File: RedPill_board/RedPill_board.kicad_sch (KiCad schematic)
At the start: 52 parts, among them J1 USB_C_Receptacle_USB2.0, J2 PROG, Q1 S9013, SW1 RESET, U1 FCM32F103CBT6, U2 STM32F401RCT6, U4 ME6211C33M5G-N, Y1 8MHz, Y2 8MHz

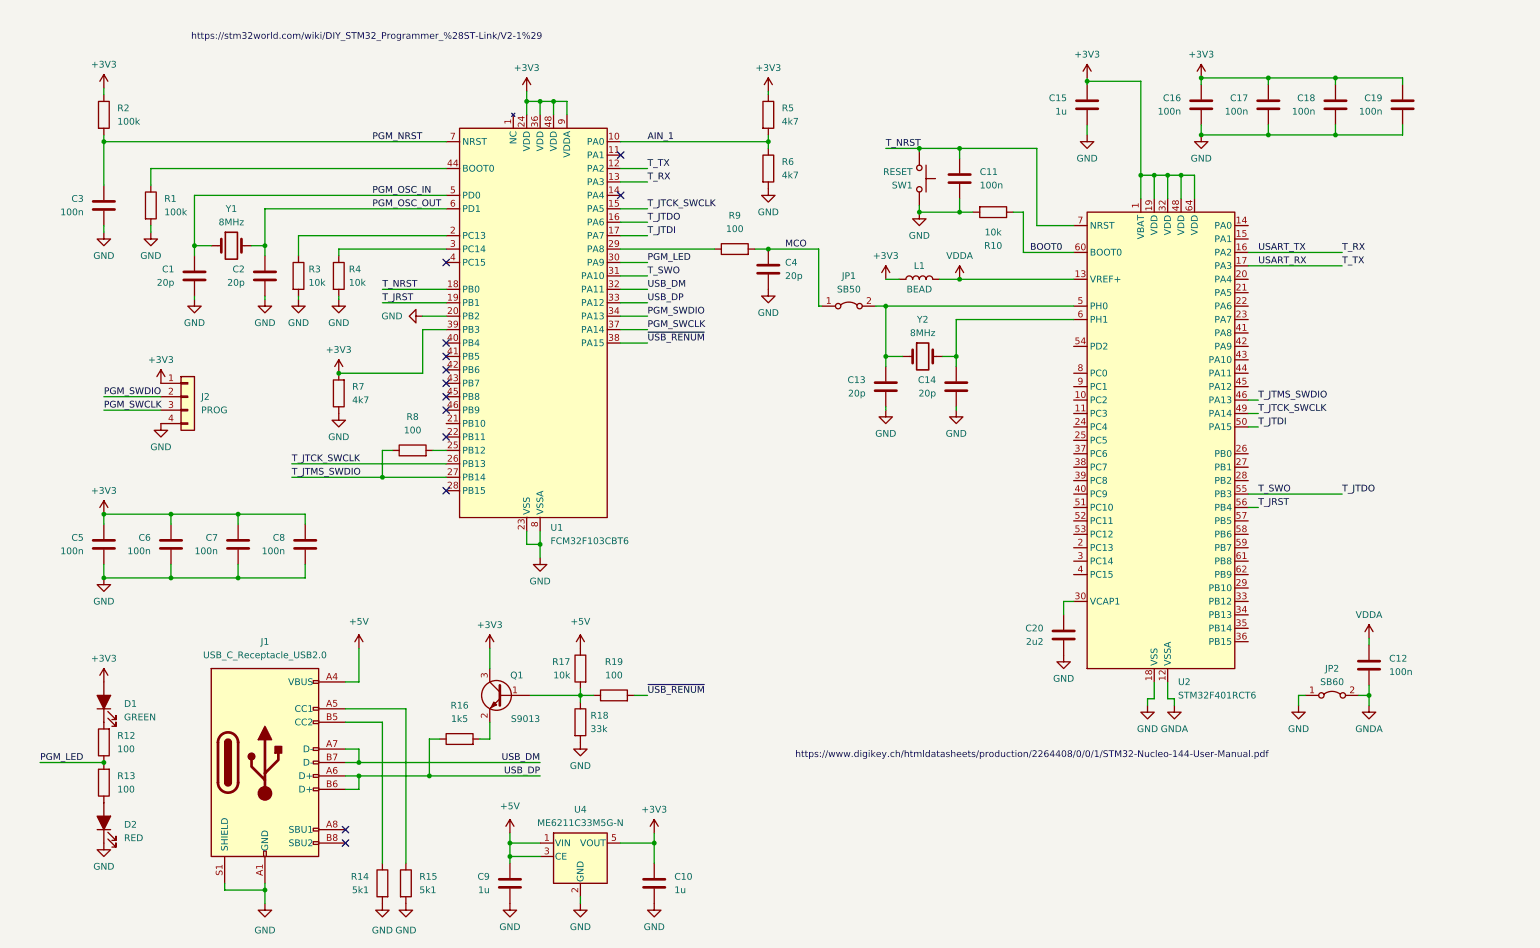
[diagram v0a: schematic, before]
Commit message: Cleanup programming nets and components, add blank connectors and initial pcb design
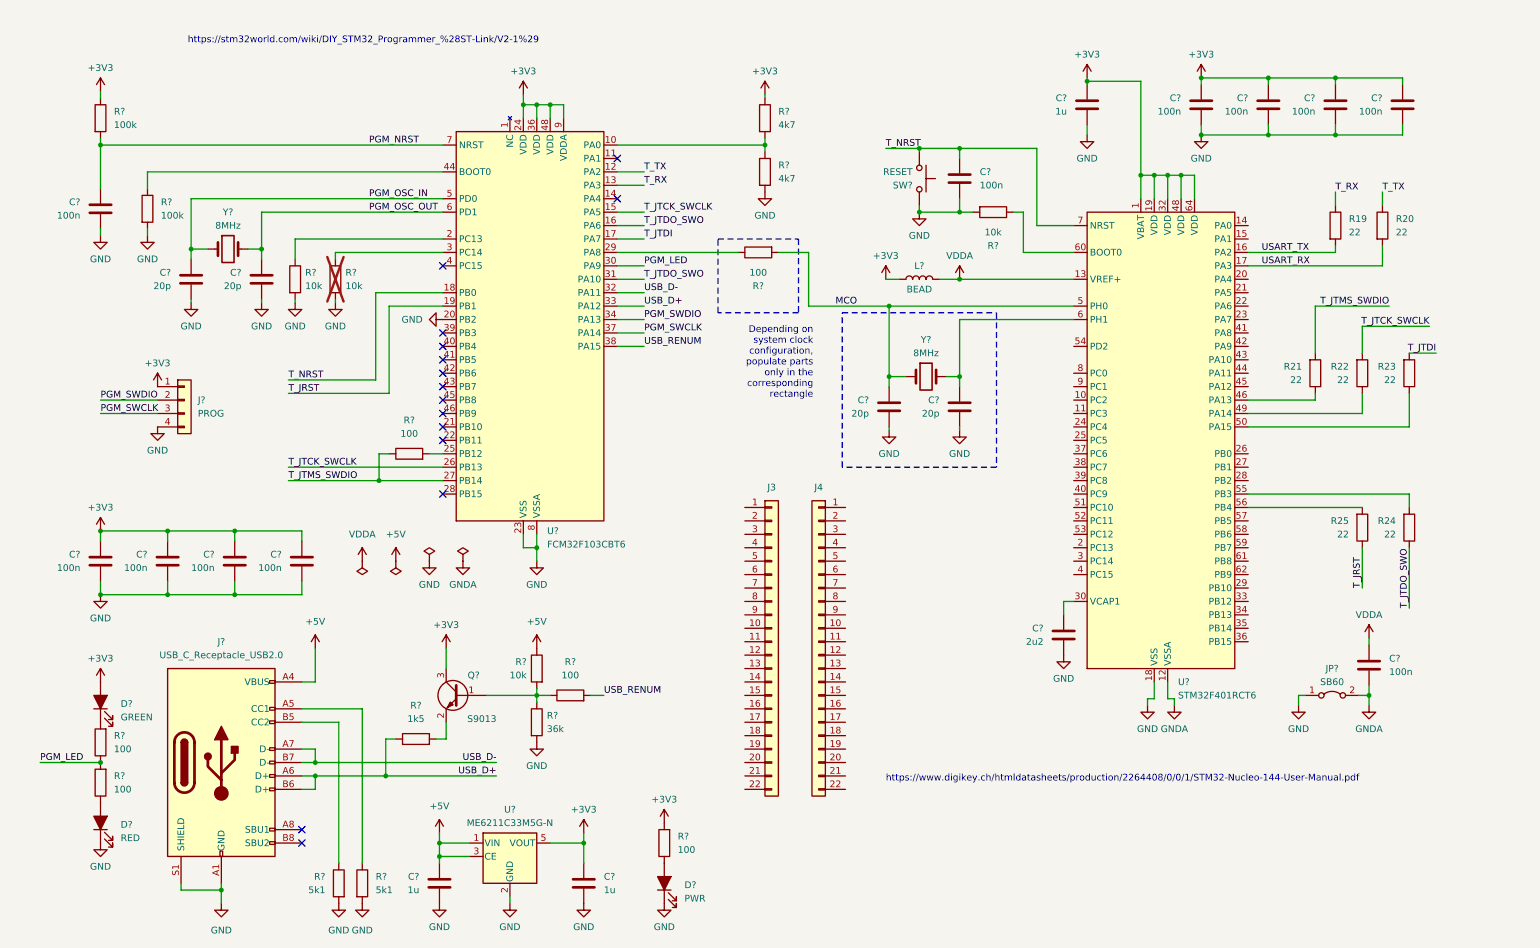
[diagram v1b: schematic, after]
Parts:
- removed C4: 20p, symbol Device:C
- removed JP1: SB50, symbol Jumper:Jumper_2_Bridged
- removed R7: 4k7, symbol Device:R
- added D?: PWR, LED_SMD:LED_0603_1608Metric, symbol Device:LED_Filled
- added J3, J4: Conn_01x22, Connector_PinHeader_2.54mm:PinHeader_1x22_P2.54mm_Vertical, symbol Connector_Generic:Conn_01x22
- added R19, R20, R21, R22, R23, R24, R25: 22, Resistor_SMD:R_0603_1608Metric, symbol Device:R
- added R?: 100, Resistor_SMD:R_0603_1608Metric, symbol Device:R
- C?: renamed from C11; footprint (none) -> Capacitor_SMD:C_0603_1608Metric
- C?: renamed from C15; footprint (none) -> Capacitor_SMD:C_0805_2012Metric
- C?: renamed from C14; footprint (none) -> Capacitor_SMD:C_0603_1608Metric
- C?: renamed from C19; footprint (none) -> Capacitor_SMD:C_0603_1608Metric
- C?: renamed from C13; footprint (none) -> Capacitor_SMD:C_0603_1608Metric
- C?: renamed from C20; footprint (none) -> Capacitor_SMD:C_0805_2012Metric
- C?: renamed from C16; footprint (none) -> Capacitor_SMD:C_0603_1608Metric
- C?: renamed from C8; footprint (none) -> Capacitor_SMD:C_0603_1608Metric
- C?: renamed from C1; footprint (none) -> Capacitor_SMD:C_0603_1608Metric
- C?: renamed from C18; footprint (none) -> Capacitor_SMD:C_0603_1608Metric
- C?: renamed from C12; footprint (none) -> Capacitor_SMD:C_0603_1608Metric
- C?: renamed from C2; footprint (none) -> Capacitor_SMD:C_0603_1608Metric
- C?: renamed from C3; footprint (none) -> Capacitor_SMD:C_0603_1608Metric
- C?: renamed from C10; footprint (none) -> Capacitor_SMD:C_0603_1608Metric
- C?: renamed from C7; footprint (none) -> Capacitor_SMD:C_0603_1608Metric
- C?: renamed from C6; footprint (none) -> Capacitor_SMD:C_0603_1608Metric
- C?: renamed from C5; footprint (none) -> Capacitor_SMD:C_0603_1608Metric
- C?: renamed from C9; footprint (none) -> Capacitor_SMD:C_0603_1608Metric
- C?: renamed from C17; footprint (none) -> Capacitor_SMD:C_0603_1608Metric
- D?: renamed from D1; footprint (none) -> LED_SMD:LED_0603_1608Metric
- D?: renamed from D2; footprint (none) -> LED_SMD:LED_0603_1608Metric
- J?: renamed from J2; footprint (none) -> Connector_PinHeader_2.54mm:PinHeader_1x04_P2.54mm_Vertical
- J?: renamed from J1; footprint jlcpcb_rotation:USB_C_Receptacle_G-Switch_GT-USB-7010ASV -> lib:USB_C_Receptacle_G-Switch_GT-USB-7010ASV
- JP?: renamed from JP2; footprint (none) -> Jumper:SolderJumper-2_P1.3mm_Open_RoundedPad1.0x1.5mm
- L?: renamed from L1; footprint (none) -> Inductor_SMD:L_0603_1608Metric
- R?: renamed from R4; footprint (none) -> Resistor_SMD:R_0603_1608Metric; now not fitted
- R?: renamed from R17; footprint (none) -> Resistor_SMD:R_0603_1608Metric
- R?: renamed from R19; footprint (none) -> Resistor_SMD:R_0603_1608Metric
- R?: renamed from R18; value 33k -> 36k; footprint (none) -> Resistor_SMD:R_0603_1608Metric
- R?: renamed from R3; footprint (none) -> Resistor_SMD:R_0603_1608Metric
- R?: renamed from R10; footprint (none) -> Resistor_SMD:R_0603_1608Metric
- R?: renamed from R1; footprint (none) -> Resistor_SMD:R_0603_1608Metric
- R?: renamed from R16; footprint (none) -> Resistor_SMD:R_0603_1608Metric
- R?: renamed from R9; footprint (none) -> Resistor_SMD:R_0603_1608Metric
- R?: renamed from R12; footprint (none) -> Resistor_SMD:R_0603_1608Metric
- R?: renamed from R13; footprint (none) -> Resistor_SMD:R_0603_1608Metric
- R?: renamed from R5; footprint (none) -> Resistor_SMD:R_0603_1608Metric
- R?: renamed from R6; footprint (none) -> Resistor_SMD:R_0603_1608Metric
- R?: renamed from R2; footprint (none) -> Resistor_SMD:R_0603_1608Metric
- R?: renamed from R8; footprint (none) -> Resistor_SMD:R_0603_1608Metric
- Y?: renamed from Y1; footprint (none) -> Crystal:Crystal_HC49-4H_Vertical
- Y?: renamed from Y2; footprint (none) -> Crystal:Crystal_HC49-4H_Vertical
- renumbered Q1 to Q?, R14 to R?, R15 to R?, SW1 to SW?, U4 to U?, U2 to U?, U1 to U?
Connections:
- net +3V3: now also R?.2; no longer U?.39 (PB3)
- net GND: now also D?.1 (K)
- net MCO: now also C?.1, U?.5 (PH0), Y?.1
- net T_JRST: now also R25.1; no longer U?.56 (PB4)
- net T_JTCK_SWCLK: now also R22.2; no longer U?.49 (PA14)
- net T_JTDI: now also R23.2; no longer U?.50 (PA15)
- net T_JTMS_SWDIO: now also R21.2; no longer U?.46 (PA13)
- net T_RX: now also R19.1; no longer U?.16 (PA2)
- net T_TX: now also R20.1; no longer U?.17 (PA3)
- net AIN_1: no longer names the net of R?.1, R?.2, U?.10 (PA0)
- net BOOT0: no longer names the net of R?.1, U?.60 (BOOT0)
- net T_JTDO renamed T_JTDO_SWO
- net T_JTDO_SWO: now also R24.1; no longer U?.55 (PB3)
- net USB_DM renamed USB_D-
- net USB_DP renamed USB_D+
- net ~{USB_RENUM} renamed USB_RENUM
- new net: D?.2 (A), R?.1
- new net: R21.1, U?.46 (PA13)
- new net: R22.1, U?.49 (PA14)
- new net: R23.1, U?.50 (PA15)
- new net: R24.2, U?.55 (PB3)
- new net: R25.2, U?.56 (PB4)
- new net USART_RX: R20.2, U?.17 (PA3)
- new net USART_TX: R19.2, U?.16 (PA2)
- no-connect marks 13 -> 15
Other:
- moved on the sheet: C?, D?, J?, Q?, R?, U?, Y?

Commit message: Minor modifications
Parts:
- removed C?: 100n, Capacitor_SMD:C_0603_1608Metric, symbol Device:C
- removed JP?: SB60, Jumper:SolderJumper-2_P1.3mm_Open_RoundedPad1.0x1.5mm, symbol Jumper:Jumper_2_Bridged
- added R?: 100k, Resistor_SMD:R_0603_1608Metric, symbol Device:R
- J?: footprint Connector_PinHeader_2.54mm:PinHeader_1x04_P2.54mm_Vertical -> Connector_PinHeader_1.27mm:PinHeader_1x04_P1.27mm_Vertical
- Y?: footprint Crystal:Crystal_HC49-4H_Vertical -> Crystal:Crystal_SMD_3225-4Pin_3.2x2.5mm
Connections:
- net GNDA is gone; now on net GND: U?.12 (VSSA)
- net +3V3: now also R?.1
- net T_NRST: now also R?.2
- net VDDA: no longer L?.2, U?.13 (VREF+)
- new net: L?.2, U?.13 (VREF+)

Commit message: Routing in progress.
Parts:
- removed C?: 100n, Capacitor_SMD:C_0603_1608Metric, symbol Device:C
- removed J3, J4: Conn_01x22, Connector_PinHeader_2.54mm:PinHeader_1x22_P2.54mm_Vertical, symbol Connector_Generic:Conn_01x22
- removed U?: ME6211C33M5G-N, Package_TO_SOT_SMD:SOT-23-5, symbol Regulator_Linear:AP2112K-3.3
- removed U?: FCM32F103CBT6, Package_QFP:LQFP-48_7x7mm_P0.5mm, symbol MCU_ST_STM32F1:STM32F103CBTx
- removed Y?: 8MHz, Crystal:Crystal_SMD_3225-4Pin_3.2x2.5mm, symbol Device:Crystal
- added C? (x2): 100n, Capacitor_SMD:C_0603_1608Metric, symbol Device:C
- added F1: 1A, Fuse:Fuse_1206_3216Metric, symbol Device:Polyfuse
- added J3, J4: Conn_01x26, Connector_PinHeader_2.54mm:PinHeader_1x26_P2.54mm_Vertical, symbol Connector_Generic:Conn_01x26
- added R27: 22, Resistor_SMD:R_0603_1608Metric, symbol Device:R
- added U1: STM32F103CBTx, Package_QFP:LQFP-48_7x7mm_P0.5mm, symbol MCU_ST_STM32F1:STM32F103CBTx
- added U2: AMS1117-3.3, Package_TO_SOT_SMD:SOT-223-3_TabPin2, symbol Regulator_Linear:AMS1117-3.3
- added Y1: 8MHz, Crystal:Crystal_SMD_3225-4Pin_3.2x2.5mm, symbol Device:Crystal_GND24
- C?: footprint Capacitor_SMD:C_0805_2012Metric -> Capacitor_SMD:C_0603_1608Metric
- R? (x3): value 100 -> 220
- R?: value 100k -> 10k
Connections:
- net +3V3: now also C?.1, J3.1 (Pin_1), J4.2 (Pin_2), U1.1 (VBAT), U1.24 (VDD), U1.36 (VDD), U1.48 (VDD), U1.9 (VDDA), U2.2 (VO)
- net +5V: now also F1.2, J4.1 (Pin_1), U2.3 (VI); no longer J?.A4 (VBUS), J?.A9 (VBUS), J?.B4 (VBUS), J?.B9 (VBUS)
- net GND: now also C?.1, C?.2, J3.14 (Pin_14), J3.26 (Pin_26), J4.26 (Pin_26), U1.20 (PB2), U1.23 (VSS), U1.35 (VSS), U1.47 (VSS), U1.8 (VSSA), U2.1 (GND), Y1.2, Y1.4
- net PGM_LED: now also U1.30 (PA9)
- net PGM_NRST: now also U1.7 (NRST)
- net PGM_OSC_IN: now also U1.5 (PD0), Y1.1
- net PGM_OSC_OUT: now also U1.6 (PD1), Y1.3
- net PGM_SWCLK: now also U1.37 (PA14)
- net PGM_SWDIO: now also U1.34 (PA13)
- net T_JRST: now also U1.19 (PB1)
- net T_JTCK_SWCLK: now also U1.15 (PA5), U1.26 (PB13)
- net T_JTDI: now also U1.17 (PA7)
- net T_JTDO_SWO: now also U1.16 (PA6), U1.31 (PA10)
- net T_JTMS_SWDIO: now also U1.27 (PB14)
- net T_NRST: now also R27.2, U1.18 (PB0); no longer R?.2, SW?.1, U?.7 (NRST)
- net T_RX: now also U1.13 (PA3)
- net T_TX: now also U1.12 (PA2)
- net USB_D+: now also U1.33 (PA12)
- net USB_D-: now also U1.32 (PA11)
- net USB_RENUM: now also U1.38 (PA15)
- net at R?.1: now also U1.3 (PC14)
- net PC2: now reaches U?.10 (PC2)
- net PC2: now also J3.20 (Pin_20)
- net PC3: now reaches U?.11 (PC3)
- net PC3: now also J3.21 (Pin_21)
- net at L?.2, U?.13 (VREF+): now also C?.2
- net PA0: now reaches U?.14 (PA0)
- net PA0: now also J3.22 (Pin_22)
- net PA1: now reaches U?.15 (PA1)
- net PA1: now also J3.23 (Pin_23)
- net PC13: now reaches U?.2 (PC13)
- net PC13: now also J3.15 (Pin_15)
- net PA4: now reaches U?.20 (PA4)
- net PA4: now also J4.25 (Pin_25)
- net PA5: now reaches U?.21 (PA5)
- net PA5: now also J4.24 (Pin_24)
- net PA6: now reaches U?.22 (PA6)
- net PA6: now also J4.23 (Pin_23)
- net PA7: now reaches U?.23 (PA7)
- net PA7: now also J4.22 (Pin_22)
- net PC4: now reaches U?.24 (PC4)
- net PC4: now also J4.21 (Pin_21)
- net PC5: now reaches U?.25 (PC5)
- net PC5: now also J4.20 (Pin_20)
- net PB0: now reaches U?.26 (PB0)
- net PB0: now also J4.19 (Pin_19)
- net PB1: now reaches U?.27 (PB1)
- net PB1: now also J4.18 (Pin_18)
- net PB2: now reaches U?.28 (PB2)
- net PB2: now also J4.17 (Pin_17)
- net PB10: now reaches U?.29 (PB10)
- net PB10: now also J4.16 (Pin_16)
- net PC14: now reaches U?.3 (PC14)
- net PC14: now also J3.16 (Pin_16)
- net PB12: now reaches U?.33 (PB12)
- net PB12: now also J4.15 (Pin_15)
- net PB13: now reaches U?.34 (PB13)
- net PB13: now also J4.14 (Pin_14)
- net PB14: now reaches U?.35 (PB14)
- net PB14: now also J4.13 (Pin_13)
- net PB15: now reaches U?.36 (PB15)
- net PB15: now also J4.12 (Pin_12)
- net PC6: now reaches U?.37 (PC6)
- net PC6: now also J4.11 (Pin_11)
- net PC7: now reaches U?.38 (PC7)
- net PC7: now also J4.10 (Pin_10)
- net PC8: now reaches U?.39 (PC8)
- net PC8: now also J4.9 (Pin_9)
- net PC15: now reaches U?.4 (PC15)
- net PC15: now also J3.17 (Pin_17)
- net PC9: now reaches U?.40 (PC9)
- net PC9: now also J4.8 (Pin_8)
- net PA8: now reaches U?.41 (PA8)
- net PA8: now also J4.7 (Pin_7)
- net PA9: now reaches U?.42 (PA9)
- net PA9: now also J4.6 (Pin_6)
- net PA10: now reaches U?.43 (PA10)
- net PA10: now also J4.5 (Pin_5)
- net PA11: now reaches U?.44 (PA11)
- net PA11: now also J4.4 (Pin_4)
- net PA12: now reaches U?.45 (PA12)
- net PA12: now also J4.3 (Pin_3)
- net PA15: now reaches R23.1, U?.50 (PA15)
- net PA15: now also J3.2 (Pin_2)
- net PC10: now reaches U?.51 (PC10)
- net PC10: now also J3.3 (Pin_3)
- net PC11: now reaches U?.52 (PC11)
- net PC11: now also J3.4 (Pin_4)
- net PC12: now reaches U?.53 (PC12)
- net PC12: now also J3.5 (Pin_5)
- net PD2: now reaches U?.54 (PD2)
- net PD2: now also J3.6 (Pin_6)
- net PB3: now reaches R24.2, U?.55 (PB3)
- net PB3: now also J3.7 (Pin_7)
- net PB4: now reaches R25.2, U?.56 (PB4)
- net PB4: now also J3.8 (Pin_8)
- net PB5: now reaches U?.57 (PB5)
- net PB5: now also J3.9 (Pin_9)
- net PB6: now reaches U?.58 (PB6)
- net PB6: now also J3.10 (Pin_10)
- net PB7: now reaches U?.59 (PB7)
- net PB7: now also J3.11 (Pin_11)
- net PB8: now reaches U?.61 (PB8)
- net PB8: now also J3.12 (Pin_12)
- net PB9: now reaches U?.62 (PB9)
- net PB9: now also J3.13 (Pin_13)
- net PC0: now reaches U?.8 (PC0)
- net PC0: now also J3.18 (Pin_18)
- net PC1: now reaches U?.9 (PC1)
- net PC1: now also J3.19 (Pin_19)
- net at R?.1: now also U1.2 (PC13)
- net at R?.1: now also U1.44 (BOOT0)
- net at R?.1: now also U1.29 (PA8)
- net at R?.1, R?.2: now also U1.10 (PA0)
- net at R?.2: now also U1.25 (PB12)
- net USART_RX renamed PA3
- net PA3: now also J3.25 (Pin_25)
- net USART_TX renamed PA2
- net PA2: now also J3.24 (Pin_24)
- new net: R27.1, R?.2, SW?.1, U?.7 (NRST)
- new net: F1.1, J?.A4 (VBUS), J?.A9 (VBUS), J?.B4 (VBUS), J?.B9 (VBUS)
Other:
- note added: "USART_RX"
- note added: "USART_TX"
- moved on the sheet: C?, L?, R?, SW?
